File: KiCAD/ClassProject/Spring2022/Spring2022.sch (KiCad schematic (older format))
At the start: 2 parts, among them U1 FUB-MINI

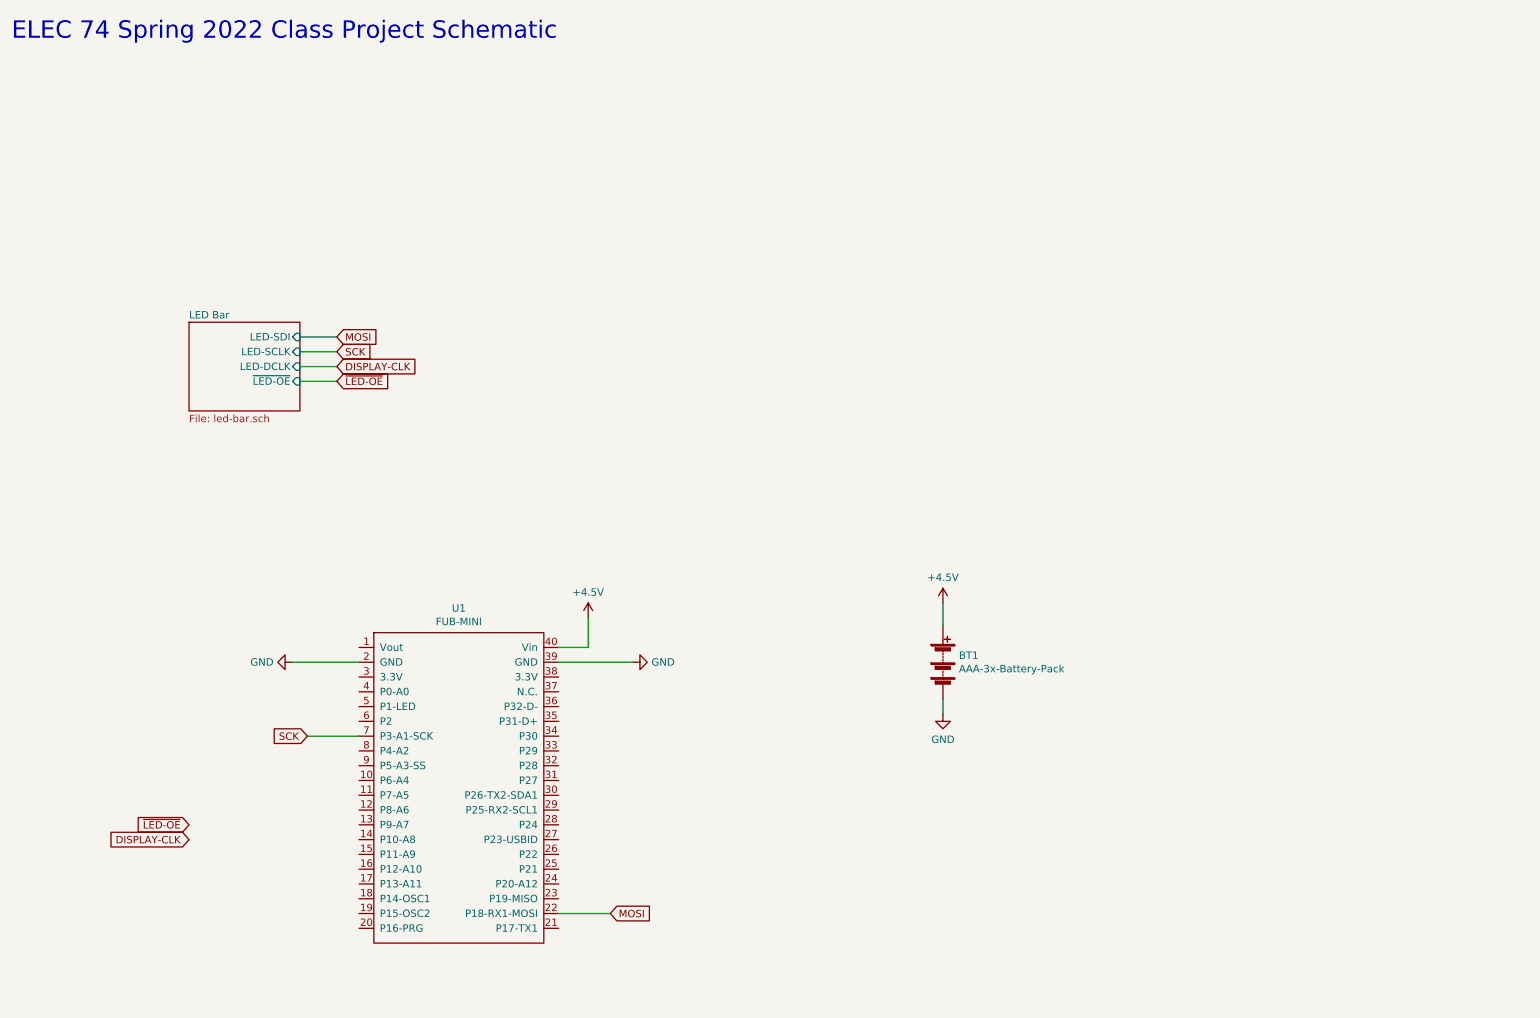
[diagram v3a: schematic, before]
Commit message: Added most other student parts.
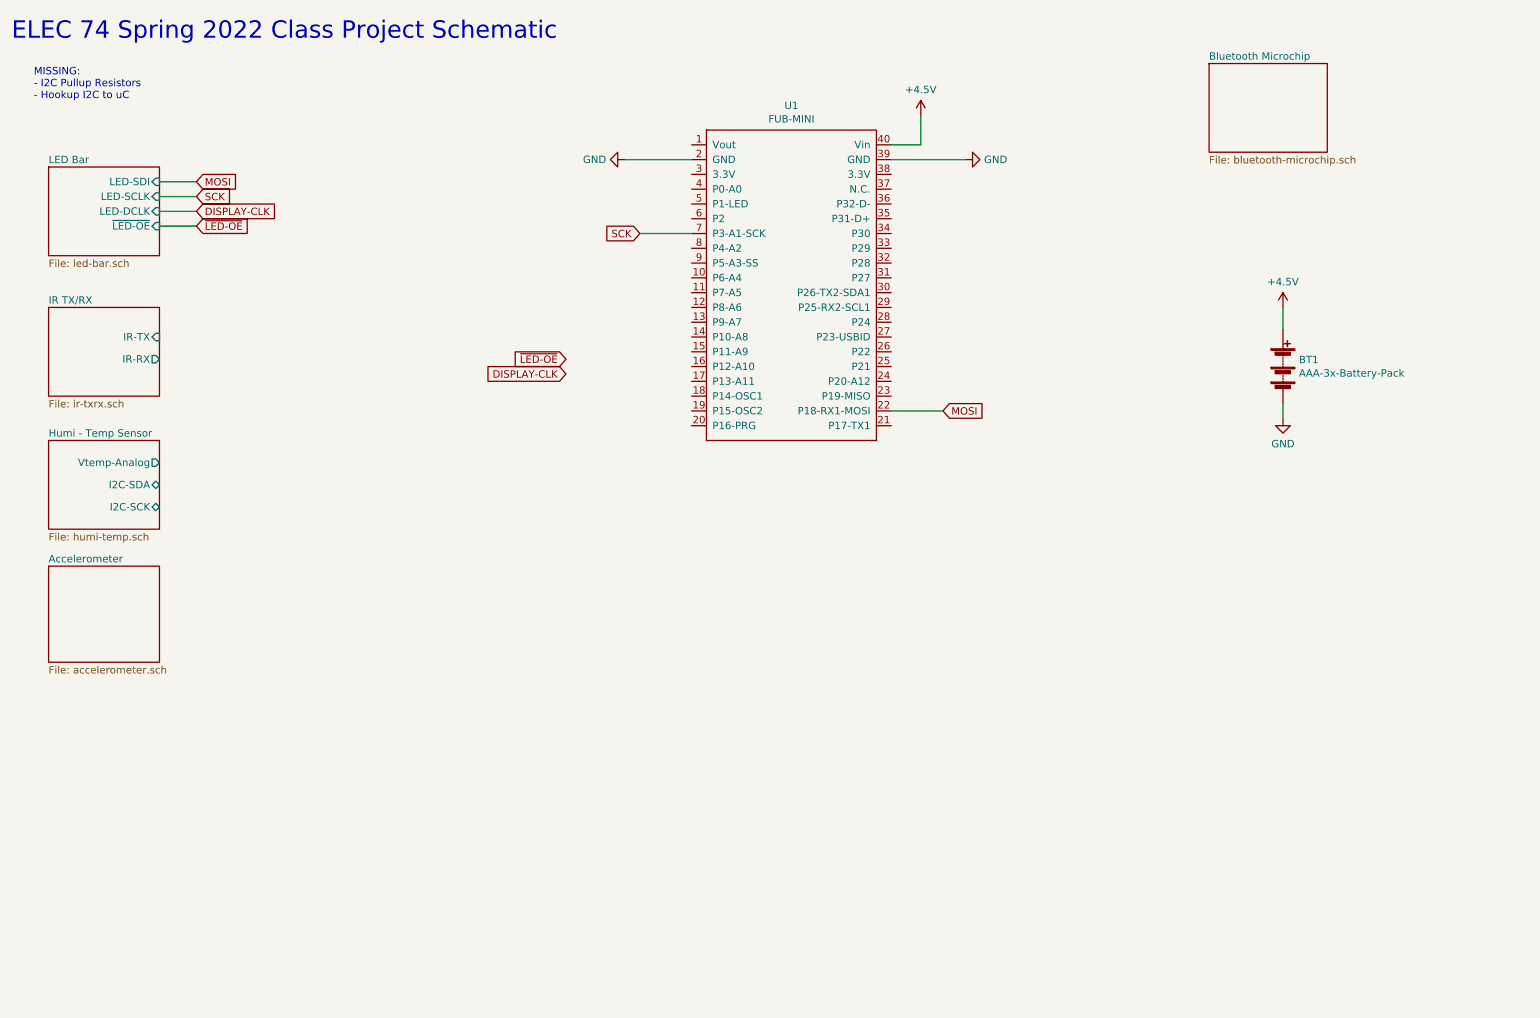
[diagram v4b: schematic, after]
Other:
- note added: "MISSING:\n- I2C Pullup Resistors\n- Hookup I2C to uC\n"
- moved on the sheet: BT1, U1
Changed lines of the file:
@@
 $Descr A4 11693 8268
 encoding utf-8
-Sheet 1 2
+Sheet 1 6
 Title ""
 Date ""
@@
 ELEC 74 Spring 2022 Class Project Schematic
 $Sheet
-S 1950 2650 750  600
+S 1000 1600 750  600
 U 625B6136
 F0 "LED Bar" 50
 F1 "led-bar.sch" 50
-F2 "LED-SDI" I R 2700 2750 50
-F3 "LED-SCLK" I R 2700 2850 50
-F4 "LED-DCLK" I R 2700 2950 50
-F5 "~LED-OE" I R 2700 3050 50
+F2 "LED-SDI" I R 1750 1700 50
+F3 "LED-SCLK" I R 1750 1800 50
+F4 "LED-DCLK" I R 1750 1900 50
+F5 "~LED-OE" I R 1750 2000 50
 $EndSheet
 $Comp
 L 74_Patrick:FUB-MINI U1
 U 1 1 625BD726
-P 3800 5650
-F 0 "U1" H 3775 6715 50  0000 C CNN
-F 1 "FUB-MINI" H 3775 6624 50  0000 C CNN
-F 2 "74_Patrick B:FubSocket_DIP-40_600_ELL" H 3600 5650 50  0001 C CNN
-F 3 "" H 3600 5650 50  0001 C CNN
-	1    3800 5650
+P 6050 2250
+F 0 "U1" H 6025 3315 50  0000 C CNN
+F 1 "FUB-MINI" H 6025 3224 50  0000 C CNN
+F 2 "74_Patrick B:FubSocket_DIP-40_600_ELL" H 5850 2250 50  0001 C CNN
+F 3 "" H 5850 2250 50  0001 C CNN
+	1    6050 2250
 	1    0    0    -1
 $EndComp
 Wire Wire Line
-	7050 5200 7050 5300
+	9350 3200 9350 3300
 $Comp
 L 74_Jacob:+4.5V #PWR0101
 U 1 1 625DDEA1
-P 7050 4550
-F 0 "#PWR0101" H 7050 4400 50  0001 C CNN
-F 1 "+4.5V" H 7050 4723 50  0000 C CNN
-F 2 "" H 7050 4550 50  0001 C CNN
-F 3 "" H 7050 4550 50  0001 C CNN
-	1    7050 4550
+P 9350 2550
+F 0 "#PWR0101" H 9350 2400 50  0001 C CNN
+F 1 "+4.5V" H 9350 2723 50  0000 C CNN
+F 2 "" H 9350 2550 50  0001 C CNN
+F 3 "" H 9350 2550 50  0001 C CNN
+	1    9350 2550
 	1    0    0    -1
 $EndComp
 Wire Wire Line
-	7050 4550 7050 4700
+	9350 2550 9350 2700
 $Comp
 L 74_Jacob:+4.5V #PWR0104
 U 1 1 625DE893
-P 4650 4650
-F 0 "#PWR0104" H 4650 4500 50  0001 C CNN
-F 1 "+4.5V" H 4650 4823 50  0000 C CNN
-F 2 "" H 4650 4650 50  0001 C CNN
-F 3 "" H 4650 4650 50  0001 C CNN
-	1    4650 4650
+P 6900 1250
+F 0 "#PWR0104" H 6900 1100 50  0001 C CNN
+F 1 "+4.5V" H 6900 1423 50  0000 C CNN
+F 2 "" H 6900 1250 50  0001 C CNN
+F 3 "" H 6900 1250 50  0001 C CNN
+	1    6900 1250
 	1    0    0    -1
 $EndComp
 Wire Wire Line
-	4650 4650 4650 4850
+	6900 1250 6900 1450
 Wire Wire Line
-	4650 4850 4450 4850
+	6900 1450 6700 1450
 $Comp
 L 74_Jacob:GND #PWR0105
 U 1 1 625DF7B3
-P 7050 5300
-F 0 "#PWR0105" H 7050 5050 50  0001 C CNN
-F 1 "GND" H 7050 5127 50  0000 C CNN
-F 2 "" H 7050 5300 50  0001 C CNN
-F 3 "" H 7050 5300 50  0001 C CNN
-	1    7050 5300
+P 9350 3300
+F 0 "#PWR0105" H 9350 3050 50  0001 C CNN
+F 1 "GND" H 9350 3127 50  0000 C CNN
+F 2 "" H 9350 3300 50  0001 C CNN
+F 3 "" H 9350 3300 50  0001 C CNN
+	1    9350 3300
 	1    0    0    -1
 $EndComp
@@
 L 74_Jacob:GND #PWR0106
 U 1 1 625DFDFE
-P 4950 4950
-F 0 "#PWR0106" H 4950 4700 50  0001 C CNN
-F 1 "GND" V 4950 4822 50  0000 R CNN
-F 2 "" H 4950 4950 50  0001 C CNN
-F 3 "" H 4950 4950 50  0001 C CNN
-	1    4950 4950
+P 7200 1550
+F 0 "#PWR0106" H 7200 1300 50  0001 C CNN
+F 1 "GND" V 7200 1422 50  0000 R CNN
+F 2 "" H 7200 1550 50  0001 C CNN
+F 3 "" H 7200 1550 50  0001 C CNN
+	1    7200 1550
 	0    -1   -1   0
 $EndComp
 Wire Wire Line
-	4950 4950 4450 4950
+	7200 1550 6700 1550
 $Comp
 L 74_Jacob:GND #PWR0107
 U 1 1 625E0E59
-P 2650 4950
-F 0 "#PWR0107" H 2650 4700 50  0001 C CNN
-F 1 "GND" V 2650 4822 50  0000 R CNN
-F 2 "" H 2650 4950 50  0001 C CNN
-F 3 "" H 2650 4950 50  0001 C CNN
-	1    2650 4950
+P 4900 1550
+F 0 "#PWR0107" H 4900 1300 50  0001 C CNN
+F 1 "GND" V 4900 1422 50  0000 R CNN
+F 2 "" H 4900 1550 50  0001 C CNN
+F 3 "" H 4900 1550 50  0001 C CNN
+	1    4900 1550
 	0    1    1    0
 $EndComp
 Wire Wire Line
-	2650 4950 3100 4950
-Text GLabel 4800 6650 2    50   Input ~ 0
+	4900 1550 5350 1550
+Text GLabel 7050 3250 2    50   Input ~ 0
 MOSI
 Wire Wire Line
-	4800 6650 4450 6650
-Text GLabel 2950 2750 2    50   Input ~ 0
+	7050 3250 6700 3250
+Text GLabel 2000 1700 2    50   Input ~ 0
 MOSI
 Wire Wire Line
-	2950 2750 2700 2750
-Text GLabel 2950 2850 2    50   Input ~ 0
+	2000 1700 1750 1700
+Text GLabel 2000 1800 2    50   Input ~ 0
 SCK
 Wire Wire Line
-	2950 2850 2700 2850
-Text GLabel 2750 5450 0    50   Input ~ 0
+	2000 1800 1750 1800
+Text GLabel 5000 2050 0    50   Input ~ 0
 SCK
 Wire Wire Line
-	2750 5450 3100 5450
-Text GLabel 2950 2950 2    50   Input ~ 0
+	5000 2050 5350 2050
+Text GLabel 2000 1900 2    50   Input ~ 0
 DISPLAY-CLK
-Text GLabel 2950 3050 2    50   Input ~ 0
+Text GLabel 2000 2000 2    50   Input ~ 0
 ~LED-OE
 Wire Wire Line
-	2950 3050 2700 3050
+	2000 2000 1750 2000
 Wire Wire Line
-	2700 2950 2950 2950
-Text GLabel 1950 6150 0    50   Input ~ 0
+	1750 1900 2000 1900
+Text GLabel 4500 3000 0    50   Input ~ 0
 DISPLAY-CLK
-Text GLabel 1950 6050 0    50   Input ~ 0
+Text GLabel 4500 2900 0    50   Input ~ 0
 ~LED-OE
 $Comp
 L 74_Jacob:AAA-3x-Battery-Pack BT1
 U 1 1 625CF271
-P 7050 4950
-F 0 "BT1" H 7158 4996 50  0000 L CNN
-F 1 "AAA-3x-Battery-Pack" H 7158 4905 50  0000 L CNN
-F 2 "74_jacob:BatteryHolder_Keystone_2479_3xAAA" V 7050 5060 50  0001 C CNN
-F 3 "~" V 7050 5060 50  0001 C CNN
-	1    7050 4950
+P 9350 2950
+F 0 "BT1" H 9458 2996 50  0000 L CNN
+F 1 "AAA-3x-Battery-Pack" H 9458 2905 50  0000 L CNN
+F 2 "74_jacob:BatteryHolder_Keystone_2479_3xAAA" V 9350 3060 50  0001 C CNN
+F 3 "~" V 9350 3060 50  0001 C CNN
+	1    9350 2950
 	1    0    0    -1
 $EndComp
+$Sheet
+S 1000 2550 750  600
+U 6265B89C
+F0 "IR TX/RX" 50
+F1 "ir-txrx.sch" 50
+F2 "IR-TX" I R 1750 2750 50
+F3 "IR-RX" O R 1750 2900 50
+$EndSheet
+$Sheet
+S 8850 900  800  600
+U 626796C5
+F0 "Bluetooth Microchip" 50
+F1 "bluetooth-microchip.sch" 50
+$EndSheet
+$Sheet
+S 1000 3450 750  600
+U 6267AD67
+F0 "Humi - Temp Sensor" 50
+F1 "humi-temp.sch" 50
+F2 "Vtemp-Analog" O R 1750 3600 50
+F3 "I2C-SDA" B R 1750 3750 50
+F4 "I2C-SCK" B R 1750 3900 50
+$EndSheet
+Text Notes 900  1150 0    50   ~ 0
+MISSING:\n- I2C Pullup Resistors\n- Hookup I2C to uC\n
+$Sheet
+S 1000 4300 750  650
+U 62691FC6
+F0 "Accelerometer" 50
+F1 "accelerometer.sch" 50
+$EndSheet
 $EndSCHEMATC

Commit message: Added decoupling caps and pull up resistors from PONTECH library
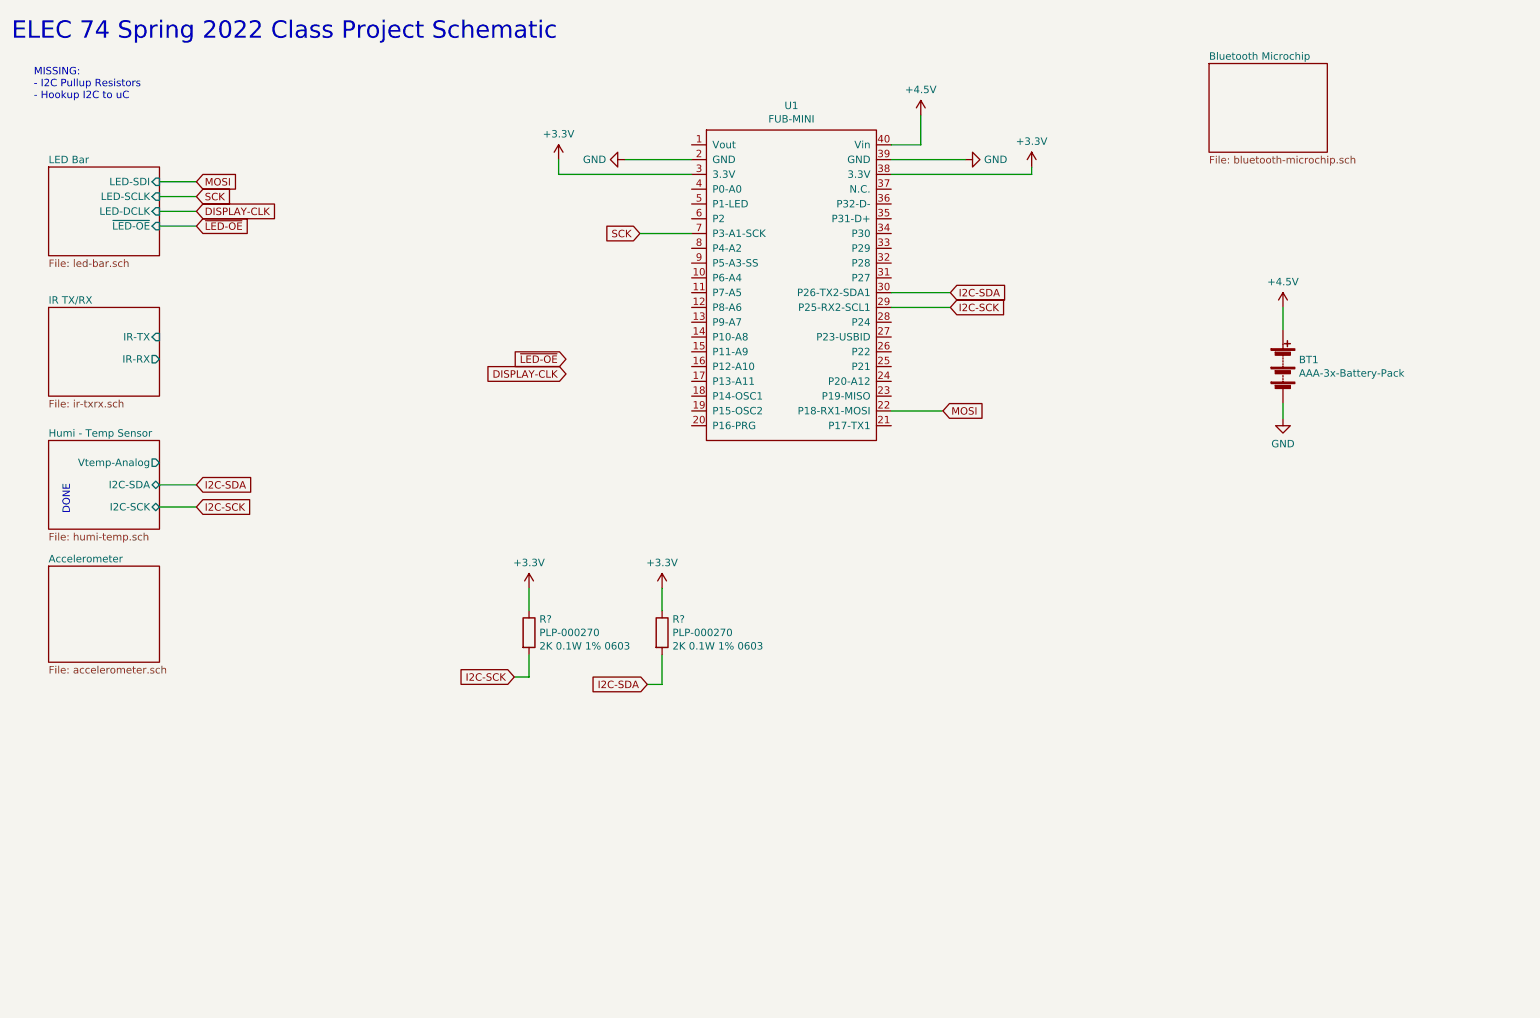
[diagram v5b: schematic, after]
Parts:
- added R? (x2): PLP-000270, a_pontech:R_0603_1608Metric, symbol 1_pontech:PLP-000270
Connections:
- net I2C-SCK: now reaches U1.29 (P25-RX2-SCL1)
- net I2C-SCK: now also R?.2
- net +3V3: now reaches U1.3 (3.3V)
- net +3V3: now also U1.38 (3.3V), R?.1, R?.1
- net I2C-SDA: now reaches U1.30 (P26-TX2-SDA1)
- net I2C-SDA: now also R?.2
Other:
- note added: "DONE"
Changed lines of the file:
@@
 F1 "accelerometer.sch" 50
 $EndSheet
+Text Notes 1150 3950 1    50   ~ 0
+DONE
+$Comp
+L 1_pontech:PLP-000270 R?
+U 1 1 626677F4
+P 4250 4750
+F 0 "R?" H 4320 4841 50  0000 L CNN
+F 1 "PLP-000270" H 4320 4750 50  0000 L CNN
+F 2 "a_pontech:R_0603_1608Metric" V 4180 4750 50  0001 C CNN
+F 3 "~" H 4250 4750 50  0001 C CNN
+F 4 "2K 0.1W 1% 0603" H 4320 4659 50  0000 L CNN "Info"
+	1    4250 4750
+	1    0    0    -1
+$EndComp
+$Comp
+L 1_pontech:PLP-000270 R?
+U 1 1 62667DF1
+P 5150 4750
+F 0 "R?" H 5220 4841 50  0000 L CNN
+F 1 "PLP-000270" H 5220 4750 50  0000 L CNN
+F 2 "a_pontech:R_0603_1608Metric" V 5080 4750 50  0001 C CNN
+F 3 "~" H 5150 4750 50  0001 C CNN
+F 4 "2K 0.1W 1% 0603" H 5220 4659 50  0000 L CNN "Info"
+	1    5150 4750
+	1    0    0    -1
+$EndComp
+$Comp
+L 74_Jacob:+3.3V #PWR?
+U 1 1 626684CA
+P 4250 4450
+F 0 "#PWR?" H 4250 4300 50  0001 C CNN
+F 1 "+3.3V" H 4250 4623 50  0000 C CNN
+F 2 "" H 4250 4450 50  0001 C CNN
+F 3 "" H 4250 4450 50  0001 C CNN
+	1    4250 4450
+	1    0    0    -1
+$EndComp
+$Comp
+L 74_Jacob:+3.3V #PWR?
+U 1 1 62668DF2
+P 5150 4450
+F 0 "#PWR?" H 5150 4300 50  0001 C CNN
+F 1 "+3.3V" H 5150 4623 50  0000 C CNN
+F 2 "" H 5150 4450 50  0001 C CNN
+F 3 "" H 5150 4450 50  0001 C CNN
+	1    5150 4450
+	1    0    0    -1
+$EndComp
+Wire Wire Line
+	5150 4450 5150 4600
+Wire Wire Line
+	4250 4450 4250 4600
+Text GLabel 4150 5050 0    50   Input ~ 0
+I2C-SCK
+Wire Wire Line
+	4150 5050 4250 5050
+Wire Wire Line
+	4250 5050 4250 4900
+Text GLabel 5050 5100 0    50   Input ~ 0
+I2C-SDA
+Wire Wire Line
+	5050 5100 5150 5100
+Wire Wire Line
+	5150 5100 5150 4900
+Text GLabel 2000 3900 2    50   Input ~ 0
+I2C-SCK
+Text GLabel 2000 3750 2    50   Input ~ 0
+I2C-SDA
+Wire Wire Line
+	2000 3750 1750 3750
+Wire Wire Line
+	1750 3900 2000 3900
+Text GLabel 7100 2450 2    50   Input ~ 0
+I2C-SDA
+Text GLabel 7100 2550 2    50   Input ~ 0
+I2C-SCK
+Wire Wire Line
+	7100 2550 6700 2550
+Wire Wire Line
+	6700 2450 7100 2450
+$Comp
+L 74_Jacob:+3.3V #PWR?
+U 1 1 6266BC1F
+P 4450 1550
+F 0 "#PWR?" H 4450 1400 50  0001 C CNN
+F 1 "+3.3V" H 4450 1723 50  0000 C CNN
+F 2 "" H 4450 1550 50  0001 C CNN
+F 3 "" H 4450 1550 50  0001 C CNN
+	1    4450 1550
+	1    0    0    -1
+$EndComp
+Wire Wire Line
+	5350 1650 4450 1650
+Wire Wire Line
+	4450 1650 4450 1550
+$Comp
+L 74_Jacob:+3.3V #PWR?
+U 1 1 6266CF06
+P 7650 1600
+F 0 "#PWR?" H 7650 1450 50  0001 C CNN
+F 1 "+3.3V" H 7650 1773 50  0000 C CNN
+F 2 "" H 7650 1600 50  0001 C CNN
+F 3 "" H 7650 1600 50  0001 C CNN
+	1    7650 1600
+	1    0    0    -1
+$EndComp
+Wire Wire Line
+	7650 1600 7650 1650
+Wire Wire Line
+	7650 1650 6700 1650
 $EndSCHEMATC
